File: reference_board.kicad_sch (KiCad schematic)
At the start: 5 parts, among them J1 CONN_02X04, U1 TMP236

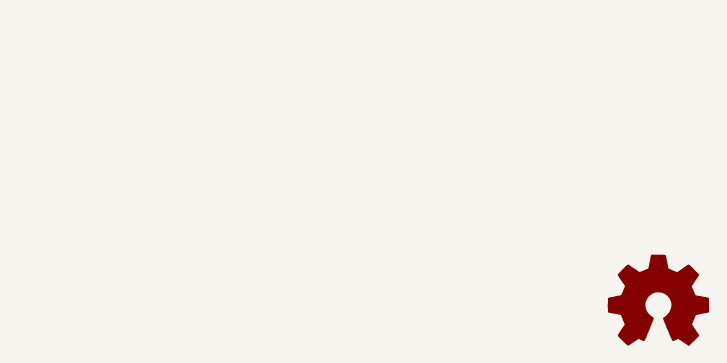
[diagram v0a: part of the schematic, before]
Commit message: Added RoHS log and APQ logo
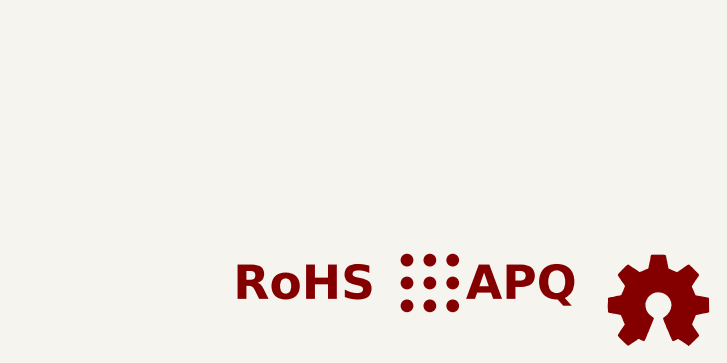
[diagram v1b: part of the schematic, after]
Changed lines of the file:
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@@
+    )
+  )
+  (symbol (lib_id "Custom_logos:Logo_APQ") (at 256.54 171.45 0) (unit 1)
+    (in_bom no) (on_board yes) (dnp no) (fields_autoplaced)
+    (property "Reference" "#LOGO1" (at 262.89 164.465 0)
+      (effects (font (size 1.27 1.27)) hide)
+    )
+    (property "Value" "Logo_APQ" (at 262.89 177.8 0)
+      (effects (font (size 1.27 1.27)) hide)
+    )
+    (property "Footprint" "" (at 264.16 171.45 0)
+      (effects (font (size 1.27 1.27)) hide)
+    )
+    (property "Datasheet" "~" (at 264.16 171.45 0)
+      (effects (font (size 1.27 1.27)) hide)
+    )
+    (property "Sim.Enable" "0" (at 256.54 171.45 0)
+      (effects (font (size 1.27 1.27)) hide)
+    )
+    (property "MFN" "" (at 256.54 171.45 0)
+      (effects (font (size 1.27 1.27)) hide)
+    )
+    (property "PN" "" (at 256.54 171.45 0)
+      (effects (font (size 1.27 1.27)) hide)
+    )
+    (instances
+      (project "reference_board"
+        (path "/afb8e687-4a13-41a1-b8c0-89a749e897fe"
+          (reference "#LOGO1") (unit 1)
+        )
+      )
+    )
+  )
+  (symbol (lib_id "Custom_logos:SYM_RoHS") (at 236.22 171.45 0) (unit 1)
+    (in_bom no) (on_board no) (dnp no) (fields_autoplaced)
+    (property "Reference" "#SYM1" (at 236.22 165.1 0)
+      (effects (font (size 1.27 1.27)) hide)
+    )
+    (property "Value" "SYM_RoHS" (at 236.22 177.8 0)
+      (effects (font (size 1.27 1.27)) hide)
+    )
+    (property "Footprint" "" (at 243.84 171.45 0)
+      (effects (font (size 1.27 1.27)) hide)
+    )
+    (property "Datasheet" "~" (at 236.22 171.45 0)
+      (effects (font (size 1.27 1.27)) hide)
+    )
+    (property "Sim.Enable" "0" (at 236.22 171.45 0)
+      (effects (font (size 1.27 1.27)) hide)
+    )
+    (instances
+      (project "reference_board"
+        (path "/afb8e687-4a13-41a1-b8c0-89a749e897fe"
+          (reference "#SYM1") (unit 1)
+        )
+      )
     )
   )
